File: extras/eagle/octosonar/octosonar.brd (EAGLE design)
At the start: 63.5 x 33 mm, 26 parts, among them IC1 PCF8574TW, IC2 74HC125D, IC3 74HC125D

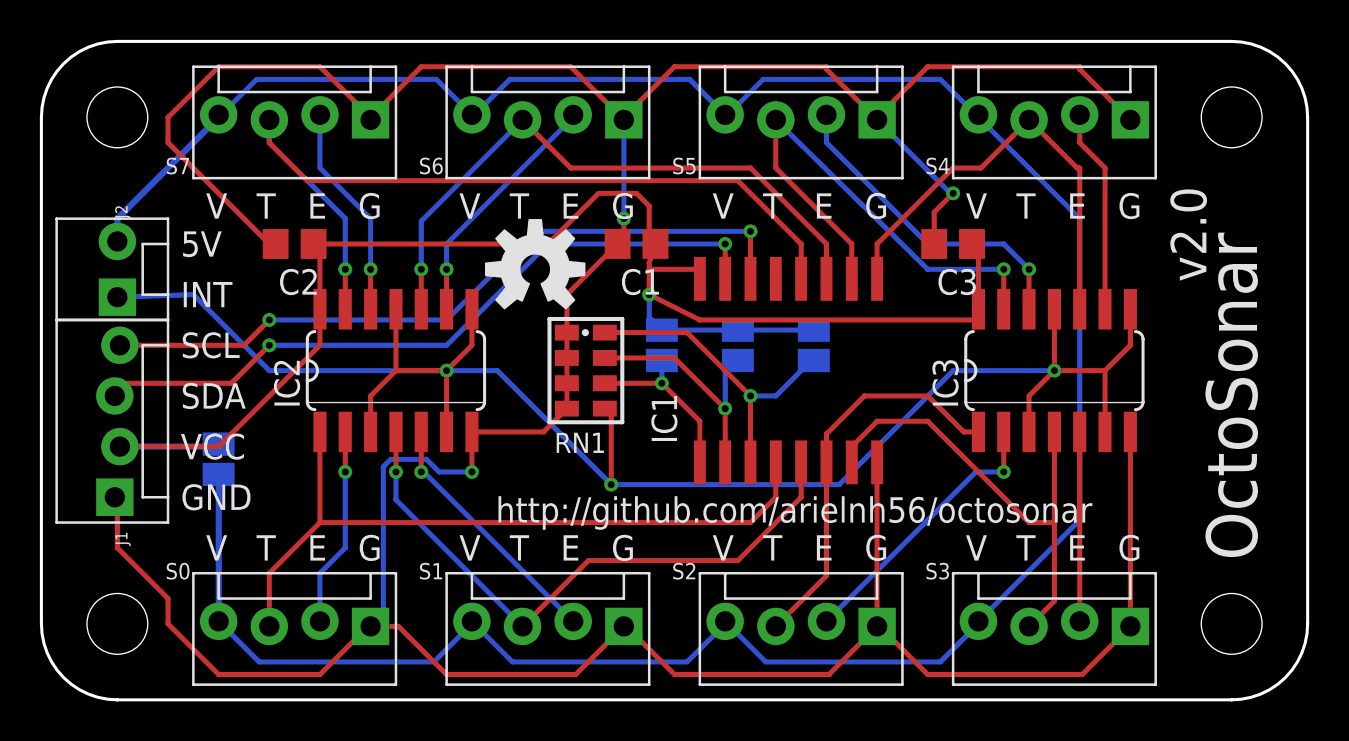
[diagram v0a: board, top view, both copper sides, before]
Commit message: octosonar board 2.1 first pass
input pins on grid
add i2c pullups
silkscreen rework
full re-route
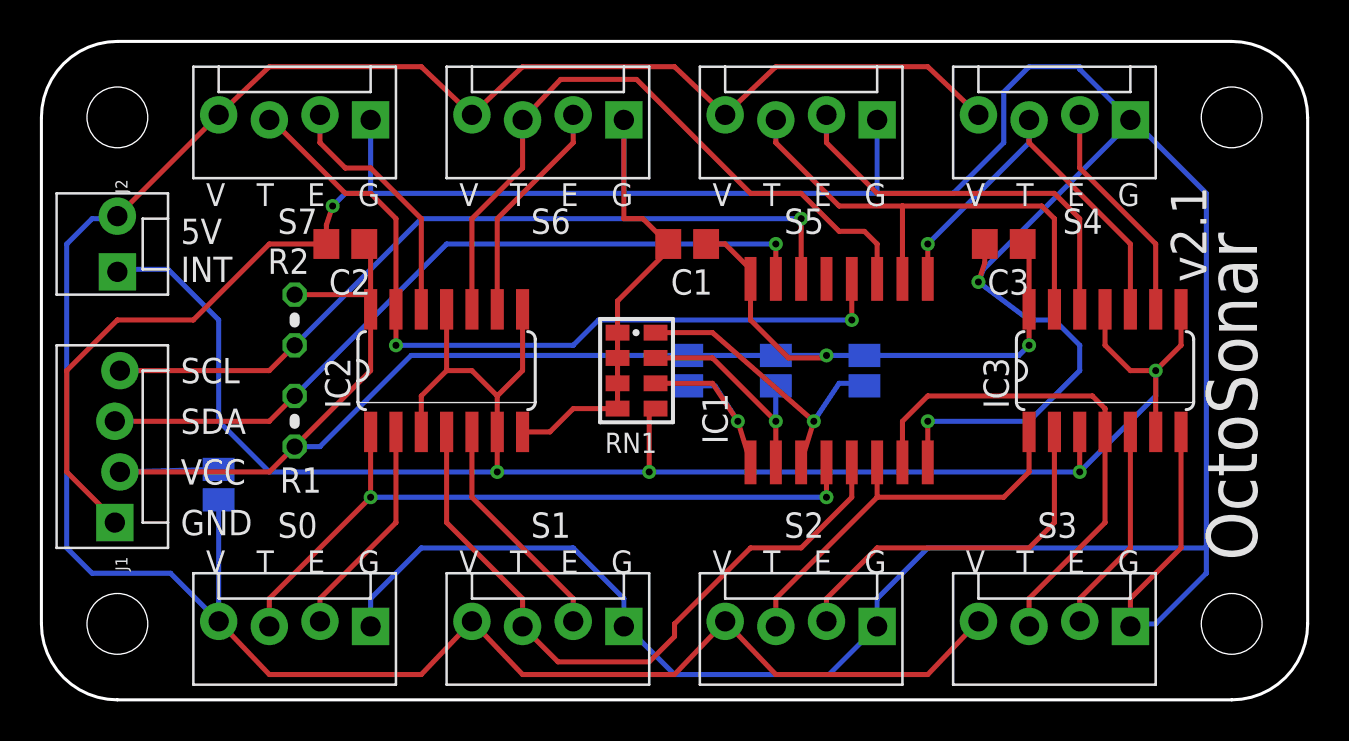
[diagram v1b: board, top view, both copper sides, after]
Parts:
- added R1, R2: (no value), rcl:0204V
- U$5: device SparkFun-Aesthetics:OSHW-LOGO-M -> SparkFun-Aesthetics:OSHW-LOGO-L
- moved U$5 29.2 mm to (54.0, 22.2), flipped to the bottom
- moved A2 2.84 mm to (41.3, 16.5)
- moved IC3 2.54 mm to (53.3, 16.5)
- moved C2 2.54 mm to (15.2, 22.9)
- moved C1 2.54 mm to (32.4, 22.9)
- moved C3 2.54 mm to (48.3, 22.9)
- moved IC1 2.54 mm to (40.0, 16.5)
- moved IC2 2.54 mm to (20.3, 16.5)
- moved RN1 2.54 mm to (29.8, 16.5)
- moved A1 2.29 mm to (36.8, 16.5)
- moved A0 1.80 mm to (32.4, 16.5)
- moved J1 1.27 mm to (3.81, 8.89)
- moved J2 1.27 mm to (3.81, 21.6)
- moved V1 1.27 mm to (8.89, 10.8)
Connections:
- net N$21: now also R2.1
- net N$22: now also R1.1
- net VCC: now also R1.2, R2.2
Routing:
- net GND: track 192.8 -> 227.9 mm
- net N$17: track 89.0 -> 97.6 mm, vias 3 -> 4
- net VCC: track 78.6 -> 85.3 mm, vias 1 -> 2
- net N$11: track 14.0 -> 18.7 mm, vias 1 -> 0
- net N$13: track 16.2 -> 20.2 mm, vias 1 -> 0
- net N$21: track 36.4 -> 40.3 mm, vias 2 -> 1
- net N$2: track 30.8 -> 34.1 mm, vias 1 -> 0
- net N$7: track 31.2 -> 34.4 mm, vias 1 -> 0
- net N$22: track 35.5 -> 38.6 mm, vias 2 -> 1
- net N$8: track 42.7 -> 40.2 mm, vias 1 -> 2
- net N$20: track 8.75 -> 10.9 mm
- net N$15: track 10.8 -> 12.6 mm, vias 1 -> 0
- net +5V: track 131.4 -> 129.8 mm
- net N$4: track 23.9 -> 25.5 mm
- net N$19: track 12.5 -> 11.2 mm
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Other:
- board text added: "v2.1"
- board text removed: "v2.0"
